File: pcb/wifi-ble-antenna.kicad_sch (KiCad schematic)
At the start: 0 parts

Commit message: Sch: Add optional antenna matching network
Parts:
- added C1, C2: C-12p-0402, DW-footprints:C_0402_1005Metric, symbol DW-capacitors:C-12p-0402
- added R1, R2: R-0R-0402, DW-footprints:R_0402_1005Metric, symbol DW-resistors:R-0R-0402
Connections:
- new net: C1.2, R1.2, R2.1
- new net: C2.2, R2.2
- new net GND: C1.1, C2.1

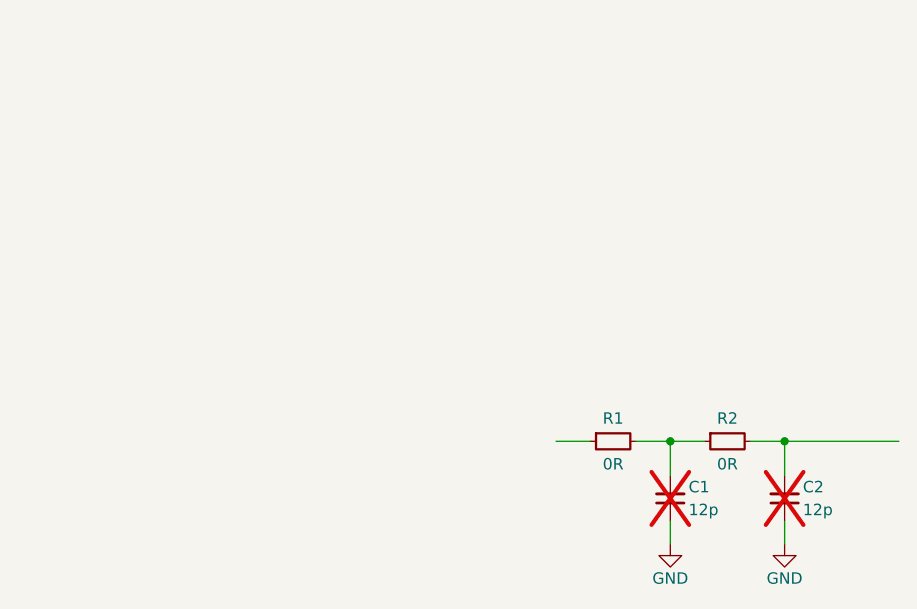
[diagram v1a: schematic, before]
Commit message: Sch: Add SMA connector and antenna, finish schematic
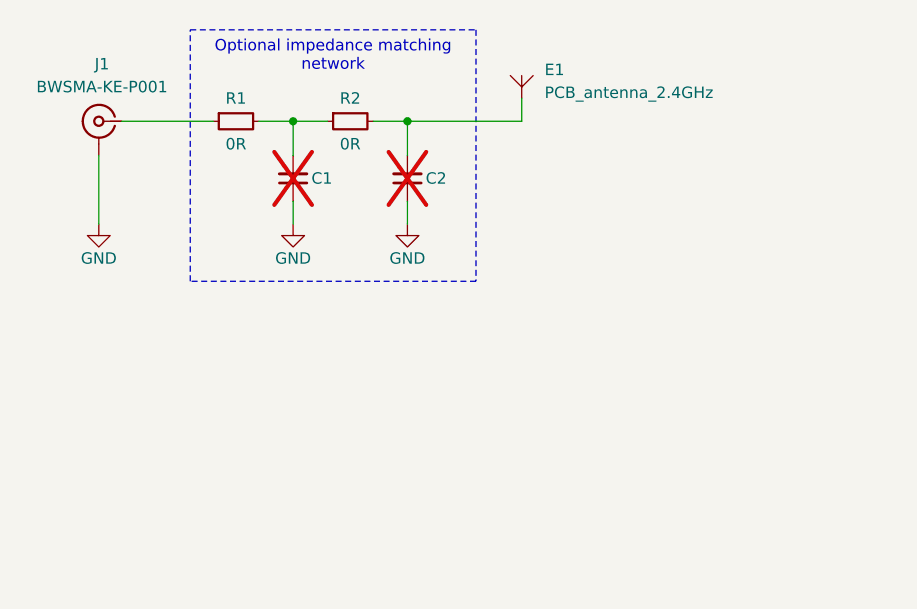
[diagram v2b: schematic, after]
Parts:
- removed C1, C2: C-12p-0402, DW-footprints:C_0402_1005Metric, symbol DW-capacitors:C-12p-0402
- added C1, C2: C-0402-template, DW-footprints:C_0402_1005Metric, symbol DW-capacitors:C-0402-template
- added E1: PCB_antenna_2.4GHz, symbol DW-mechanical:PCB_antenna_2.4GHz
- added J1: BWSMA-KE-P001, DW-footprints:Conn_SMA_BWSMA-KE-P001, symbol DW-connectors:SMA_BWSMA-KE-P001
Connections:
- net GND: now also C1.1, C2.1, J1.2
- net at R1.1: now also J1.1
- net at R1.2, R2.1: now also C1.2
- net at R2.2: now also C2.2, E1.1
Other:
- moved on the sheet: R1, R2

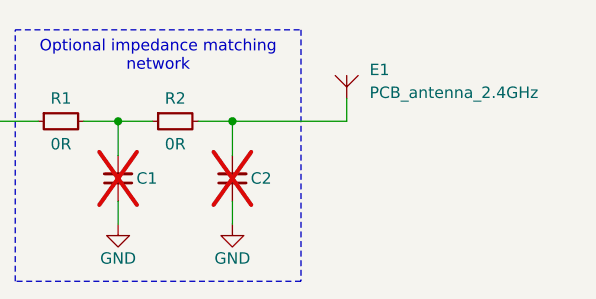
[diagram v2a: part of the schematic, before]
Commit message: PCB: Define stackup and pre-defined sizes, init PCB layout
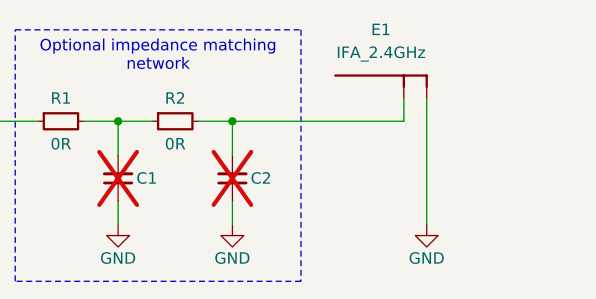
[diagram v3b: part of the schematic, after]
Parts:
- removed E1: PCB_antenna_2.4GHz, symbol DW-mechanical:PCB_antenna_2.4GHz
- added E1: IFA_2.4GHz, DW-footprints:Antenna_Custom_IFA_2.4GHz, symbol DW-mechanical:IFA_2.4GHz
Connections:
- net GND: now also E1.2 (GND)
- net at C2.2, R2.2: now also E1.1 (SIG)
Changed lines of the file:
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@@
+	(wire
+		(pts
+			(xy 132.08 63.5) (xy 132.08 77.47)
+		)
+		(stroke
+			(width 0)
+			(type default)
+		)
+	)
 	(wire
 		(pts
@@
 	(wire
 		(pts
-			(xy 123.19 63.5) (xy 123.19 66.04)
+			(xy 129.54 66.04) (xy 129.54 63.5)
 		)
 		(stroke
@@
 	(wire
 		(pts
-			(xy 110.49 66.04) (xy 123.19 66.04)
-		)
-		(stroke
-			(width 0)
-			(type default)
-		)
-	)
-	(wire
-		(pts
 			(xy 97.79 66.04) (xy 97.79 69.85)
 		)
@@
 		(pts
 			(xy 110.49 74.93) (xy 110.49 77.47)
+		)
+		(stroke
+			(width 0)
+			(type default)
+		)
+	)
+	(wire
+		(pts
+			(xy 110.49 66.04) (xy 129.54 66.04)
 		)
 		(stroke
@@
 	(symbol
 		(lib_id "DW-power-symbols:GND")
+		(at 132.08 77.47 0)
+		(unit 1)
+		(exclude_from_sim no)
+		(in_bom yes)
+		(on_board yes)
+		(dnp no)
+		(property "Reference" "#PWR04"
+			(at 132.08 83.82 0)
+			(effects
+				(font
+					(size 1.27 1.27)
+				)
+				(hide yes)
+			)
+		)
+		(property "Value" "GND"
+			(at 132.08 81.28 0)
+			(effects
+				(font
+					(size 1.27 1.27)
+				)
+			)
+		)
+		(property "Footprint" ""
+			(at 132.08 77.47 0)
+			(effects
+				(font
+					(size 1.27 1.27)
+				)
+				(hide yes)
+			)
+		)
+		(property "Datasheet" ""
+			(at 132.08 77.47 0)
+			(effects
+				(font
+					(size 1.27 1.27)
+				)
+				(hide yes)
+			)
+		)
+		(property "Description" "Power symbol creates a global label with name \"GND\" , ground"
+			(at 132.08 77.47 0)
+			(effects
+				(font
+					(size 1.27 1.27)
+				)
+				(hide yes)
+			)
+		)
+		(pin "1"
+		)
+		(instances
+			(project "wifi-ble-antenna"
+				(path "/15beafc1-24d5-45e3-95c8-dabbbcd946d2"
+					(reference "#PWR04")
+					(unit 1)
+				)
+			)
+		)
+	)
+	(symbol
+		(lib_id "DW-power-symbols:GND")
 		(at 76.2 77.47 0)
 		(unit 1)
@@
 				(path "/15beafc1-24d5-45e3-95c8-dabbbcd946d2"
 					(reference "#PWR03")
-					(unit 1)
-				)
-			)
-		)
-	)
-	(symbol
-		(lib_id "DW-mechanical:PCB_antenna_2.4GHz")
-		(at 123.19 60.96 0)
-		(unit 1)
-		(exclude_from_sim no)
-		(in_bom yes)
-		(on_board yes)
-		(dnp no)
-		(fields_autoplaced yes)
-		(property "Reference" "E1"
-			(at 125.73 60.325 0)
-			(effects
-				(font
-					(size 1.27 1.27)
-					(thickness 0.15)
-				)
-				(justify left)
-			)
-		)
-		(property "Value" "PCB_antenna_2.4GHz"
-			(at 125.73 62.865 0)
-			(effects
-				(font
-					(size 1.27 1.27)
-					(thickness 0.15)
-				)
-				(justify left)
-			)
-		)
-		(property "Footprint" ""
-			(at 125.73 66.04 0)
-			(effects
-				(font
-					(size 1.27 1.27)
-					(thickness 0.15)
-				)
-				(justify left bottom)
-				(hide yes)
-			)
-		)
-		(property "Datasheet" ""
-			(at 125.73 68.58 0)
-			(effects
-				(font
-					(size 1.27 1.27)
-					(thickness 0.15)
-				)
-				(justify left bottom)
-				(hide yes)
-			)
-		)
-		(property "Description" ""
-			(at 125.73 71.12 0)
-			(effects
-				(font
-					(size 1.27 1.27)
-					(thickness 0.15)
-				)
-				(justify left bottom)
-				(hide yes)
-			)
-		)
-		(pin "1"
-		)
-		(instances
-			(project ""
-				(path "/15beafc1-24d5-45e3-95c8-dabbbcd946d2"
-					(reference "E1")
 					(unit 1)
 				)
@@
 					(unit 1)
 				)
+			)
+		)
+	)
+	(symbol
+		(lib_id "DW-mechanical:IFA_2.4GHz")
+		(at 129.54 62.23 0)
+		(mirror y)
+		(unit 1)
+		(exclude_from_sim no)
+		(in_bom yes)
+		(on_board yes)
+		(dnp no)
+		(property "Reference" "E1"
+			(at 127 55.88 0)
+			(effects
+				(font
+					(size 1.27 1.27)
+					(thickness 0.15)
+				)
+			)
+		)
+		(property "Value" "IFA_2.4GHz"
+			(at 127 58.42 0)
+			(effects
+				(font
+					(size 1.27 1.27)
+					(thickness 0.15)
+				)
+			)
+		)
+		(property "Footprint" "DW-footprints:Antenna_Custom_IFA_2.4GHz"
+			(at 124.46 67.31 0)
+			(effects
+				(font
+					(size 1.27 1.27)
+					(thickness 0.15)
+				)
+				(justify left bottom)
+				(hide yes)
+			)
+		)
+		(property "Datasheet" ""
+			(at 127 69.85 0)
+			(effects
+				(font
+					(size 1.27 1.27)
+					(thickness 0.15)
+				)
+				(justify left bottom)
+				(hide yes)
+			)
+		)
+		(property "Description" "2.4GHz PCB Inverted-F Antenna"
+			(at 124.46 72.39 0)
+			(effects
+				(font
+					(size 1.27 1.27)
+					(thickness 0.15)
+				)
+				(justify left bottom)
+				(hide yes)
+			)
+		)
+		(pin "1"
+		)
+		(pin "2"
+		)
+		(instances
+			(project ""
+				(path "/15beafc1-24d5-45e3-95c8-dabbbcd946d2"
+					(reference "E1")
+					(unit 1)
+				)

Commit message: PCB: Finalize layout - add impedance matching geometry to SMA, ensure dimensions are as designed
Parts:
- E1: now left out of the parts list
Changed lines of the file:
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@@
 		(unit 1)
 		(exclude_from_sim no)
-		(in_bom yes)
+		(in_bom no)
 		(on_board yes)
 		(dnp no)
